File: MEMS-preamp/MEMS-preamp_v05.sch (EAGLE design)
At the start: 19 parts, among them Q1 OPA2134

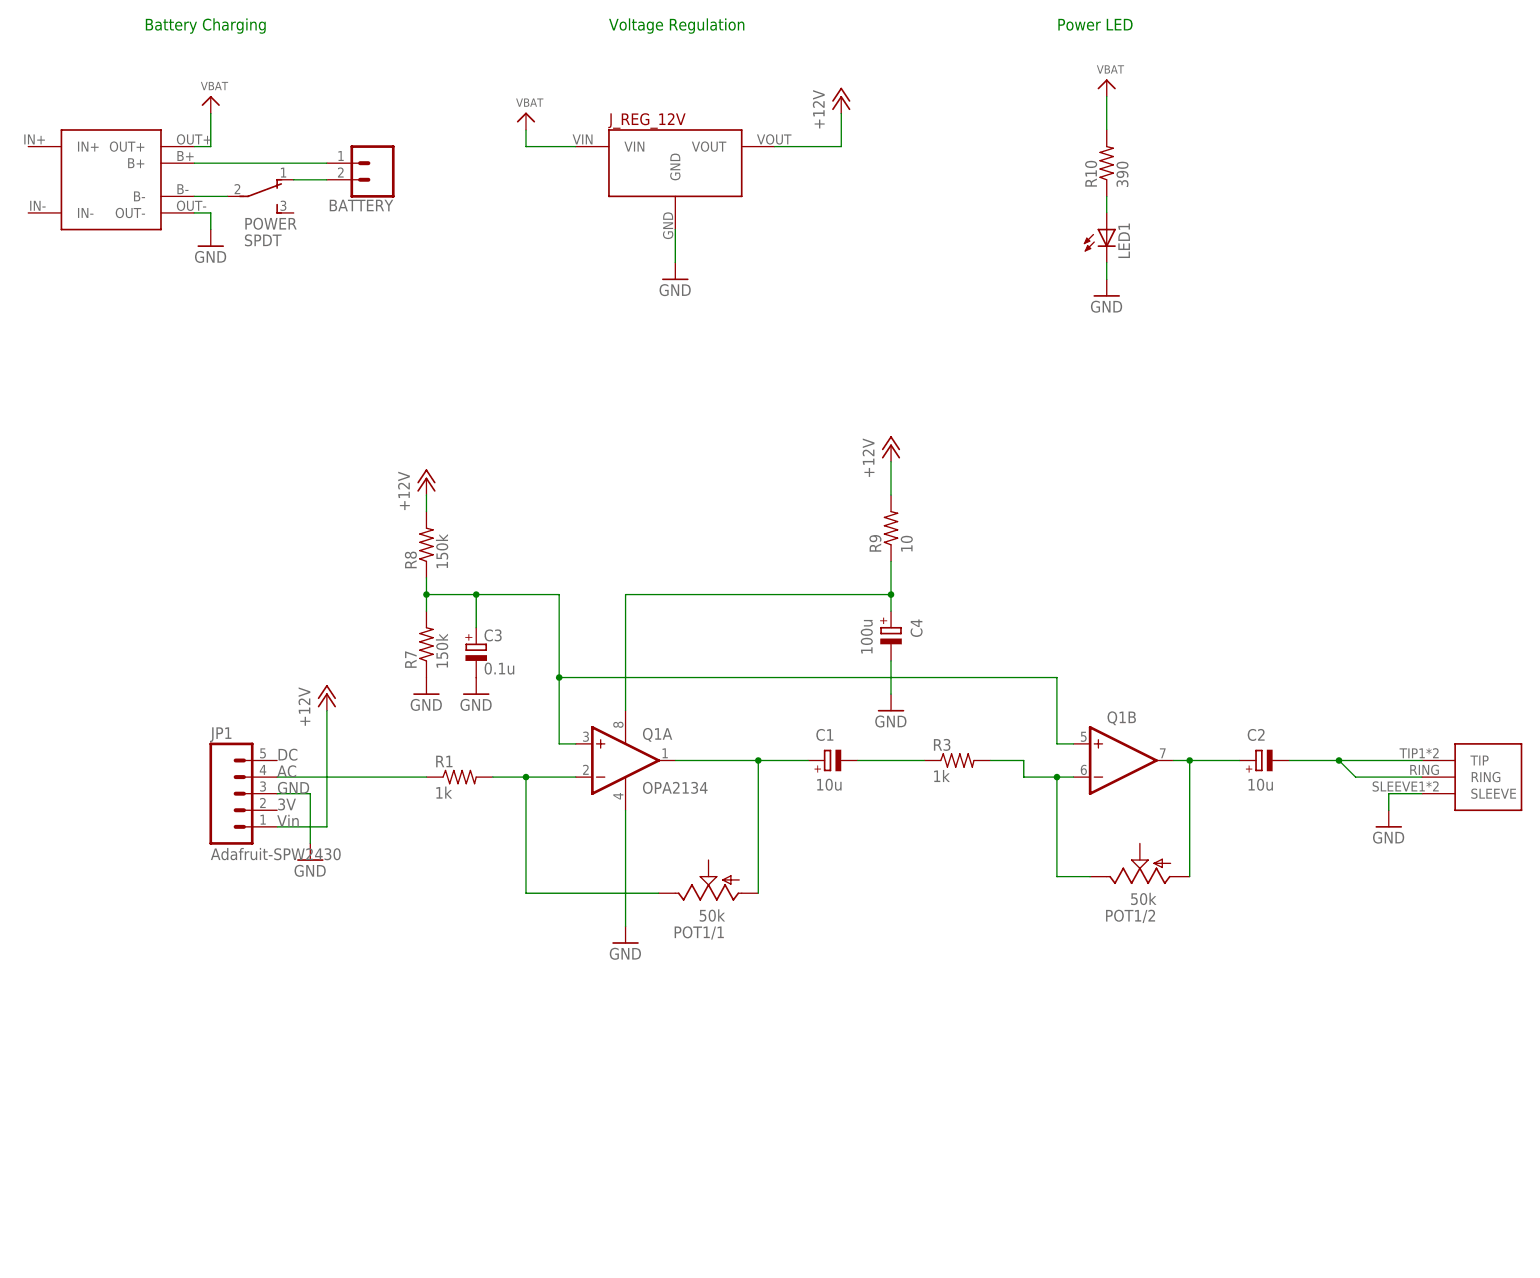
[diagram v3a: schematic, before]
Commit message: new piezo preamp designs
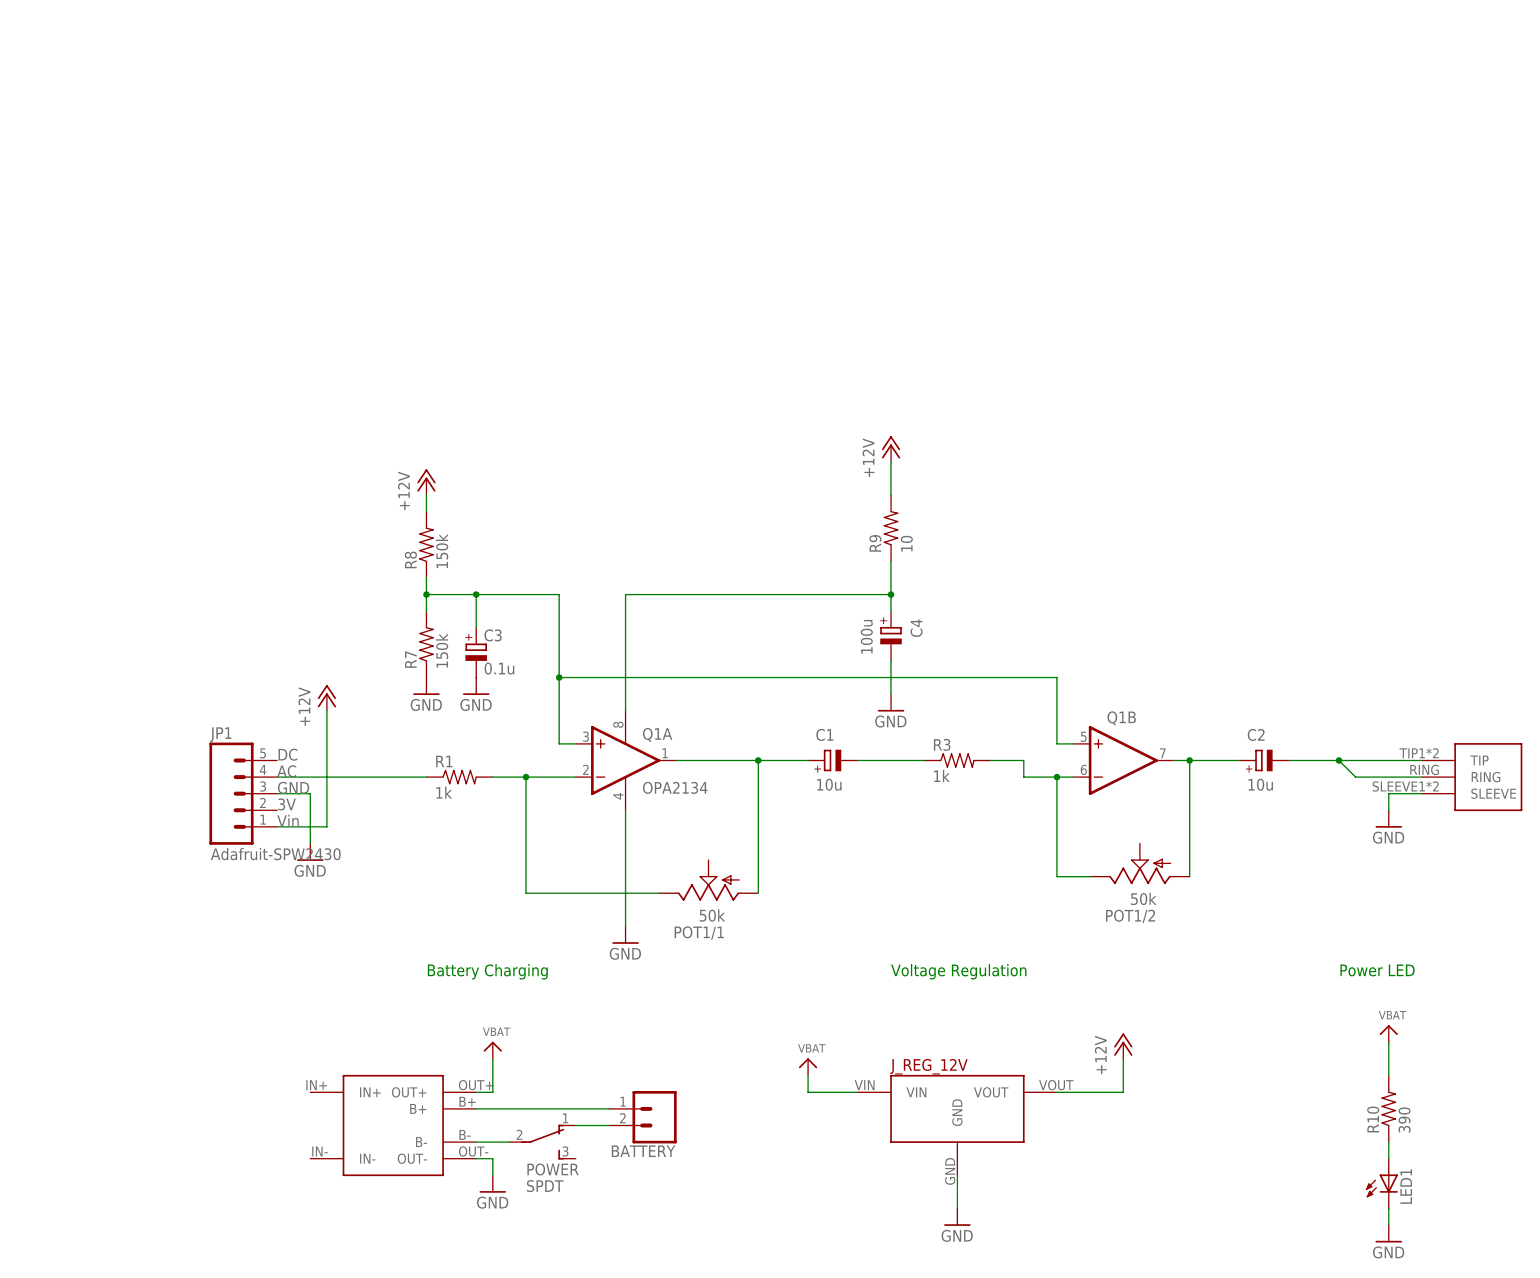
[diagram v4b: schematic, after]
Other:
- moved on the sheet: BATTERY, J_REG_12V, LED1, POWER, R10
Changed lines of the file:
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@@
 <sheet>
 <plain>
-<text x="66.04" y="182.88" size="1.778" layer="91">Voltage Regulation</text>
-<text x="-5.08" y="182.88" size="1.778" layer="91">Battery Charging</text>
-<text x="134.62" y="182.88" size="1.778" layer="91">Power LED</text>
+<text x="109.22" y="38.1" size="1.778" layer="91">Voltage Regulation</text>
+<text x="38.1" y="38.1" size="1.778" layer="91">Battery Charging</text>
+<text x="177.8" y="38.1" size="1.778" layer="91">Power LED</text>
 </plain>
 <instances>
@@
 <attribute name="VALUE" x="182.88" y="58.42" size="1.778" layer="96" ratio="12"/>
 </instance>
-<instance part="LED1" gate="G$1" x="142.24" y="152.4"/>
-<instance part="GND1" gate="1" x="142.24" y="142.24" smashed="yes">
-<attribute name="VALUE" x="139.7" y="139.7" size="1.778" layer="96" ratio="12"/>
-</instance>
-<instance part="R10" gate="G$1" x="142.24" y="162.56" rot="R90"/>
-<instance part="J_REG_12V" gate="J_REG_5V" x="76.2" y="165.1"/>
-<instance part="GND12" gate="1" x="76.2" y="144.78" smashed="yes">
-<attribute name="VALUE" x="73.66" y="142.24" size="1.778" layer="96" ratio="12"/>
-</instance>
-<instance part="U$2" gate="G$1" x="53.34" y="170.18"/>
-<instance part="P+1" gate="1" x="101.6" y="172.72"/>
-<instance part="U$3" gate="G$1" x="142.24" y="175.26"/>
+<instance part="LED1" gate="G$1" x="185.42" y="7.62"/>
+<instance part="GND1" gate="1" x="185.42" y="-2.54" smashed="yes">
+<attribute name="VALUE" x="182.88" y="-5.08" size="1.778" layer="96" ratio="12"/>
+</instance>
+<instance part="R10" gate="G$1" x="185.42" y="17.78" rot="R90"/>
+<instance part="J_REG_12V" gate="J_REG_5V" x="119.38" y="20.32"/>
+<instance part="GND12" gate="1" x="119.38" y="0" smashed="yes">
+<attribute name="VALUE" x="116.84" y="-2.54" size="1.778" layer="96" ratio="12"/>
+</instance>
+<instance part="U$2" gate="G$1" x="96.52" y="25.4"/>
+<instance part="P+1" gate="1" x="144.78" y="27.94"/>
+<instance part="U$3" gate="G$1" x="185.42" y="30.48"/>
 <instance part="P+5" gate="1" x="109.22" y="119.38"/>
-<instance part="USB-LIPO-CHARGER" gate="G$1" x="-10.16" y="160.02"/>
-<instance part="U$8" gate="G$1" x="5.08" y="172.72"/>
-<instance part="GND13" gate="1" x="5.08" y="149.86" smashed="yes">
-<attribute name="VALUE" x="2.54" y="147.32" size="1.778" layer="96" ratio="12"/>
+<instance part="USB-LIPO-CHARGER" gate="G$1" x="33.02" y="15.24"/>
+<instance part="U$8" gate="G$1" x="48.26" y="27.94"/>
+<instance part="GND13" gate="1" x="48.26" y="5.08" smashed="yes">
+<attribute name="VALUE" x="45.72" y="2.54" size="1.778" layer="96" ratio="12"/>
 </instance>
 <instance part="P+6" gate="1" x="38.1" y="114.3"/>
-<instance part="POWER" gate="G$1" x="12.7" y="157.48"/>
+<instance part="POWER" gate="G$1" x="55.88" y="12.7"/>
 <instance part="P+2" gate="1" x="22.86" y="81.28"/>
-<instance part="BATTERY" gate="G$1" x="30.48" y="162.56" rot="R180"/>
+<instance part="BATTERY" gate="G$1" x="73.66" y="17.78" rot="R180"/>
 <instance part="R3" gate="G$1" x="119.38" y="71.12"/>
 <instance part="C2" gate="G$1" x="165.1" y="71.12" smashed="yes" rot="R90">
@@
 <pinref part="LED1" gate="G$1" pin="C"/>
 <pinref part="GND1" gate="1" pin="GND"/>
-<wire x1="142.24" y1="147.32" x2="142.24" y2="144.78" width="0.1524" layer="91"/>
+<wire x1="185.42" y1="2.54" x2="185.42" y2="0" width="0.1524" layer="91"/>
 </segment>
 <segment>
 <pinref part="J_REG_12V" gate="J_REG_5V" pin="GND"/>
 <pinref part="GND12" gate="1" pin="GND"/>
-<wire x1="76.2" y1="152.4" x2="76.2" y2="147.32" width="0.1524" layer="91"/>
+<wire x1="119.38" y1="7.62" x2="119.38" y2="2.54" width="0.1524" layer="91"/>
 </segment>
 <segment>
 <pinref part="USB-LIPO-CHARGER" gate="G$1" pin="OUT-"/>
 <pinref part="GND13" gate="1" pin="GND"/>
-<wire x1="2.54" y1="154.94" x2="5.08" y2="154.94" width="0.1524" layer="91"/>
-<wire x1="5.08" y1="154.94" x2="5.08" y2="152.4" width="0.1524" layer="91"/>
+<wire x1="45.72" y1="10.16" x2="48.26" y2="10.16" width="0.1524" layer="91"/>
+<wire x1="48.26" y1="10.16" x2="48.26" y2="7.62" width="0.1524" layer="91"/>
 </segment>
 </net>
@@
 <pinref part="U$2" gate="G$1" pin="VBAT"/>
 <pinref part="J_REG_12V" gate="J_REG_5V" pin="VIN"/>
-<wire x1="53.34" y1="167.64" x2="53.34" y2="165.1" width="0.1524" layer="91"/>
-<wire x1="53.34" y1="165.1" x2="60.96" y2="165.1" width="0.1524" layer="91"/>
+<wire x1="96.52" y1="22.86" x2="96.52" y2="20.32" width="0.1524" layer="91"/>
+<wire x1="96.52" y1="20.32" x2="104.14" y2="20.32" width="0.1524" layer="91"/>
 </segment>
 <segment>
 <pinref part="R10" gate="G$1" pin="2"/>
 <pinref part="U$3" gate="G$1" pin="VBAT"/>
-<wire x1="142.24" y1="167.64" x2="142.24" y2="172.72" width="0.1524" layer="91"/>
+<wire x1="185.42" y1="22.86" x2="185.42" y2="27.94" width="0.1524" layer="91"/>
 </segment>
 <segment>
 <pinref part="USB-LIPO-CHARGER" gate="G$1" pin="OUT+"/>
 <pinref part="U$8" gate="G$1" pin="VBAT"/>
-<wire x1="2.54" y1="165.1" x2="5.08" y2="165.1" width="0.1524" layer="91"/>
-<wire x1="5.08" y1="165.1" x2="5.08" y2="170.18" width="0.1524" layer="91"/>
+<wire x1="45.72" y1="20.32" x2="48.26" y2="20.32" width="0.1524" layer="91"/>
+<wire x1="48.26" y1="20.32" x2="48.26" y2="25.4" width="0.1524" layer="91"/>
 </segment>
 </net>
@@
 <pinref part="R10" gate="G$1" pin="1"/>
 <pinref part="LED1" gate="G$1" pin="A"/>
-<wire x1="142.24" y1="157.48" x2="142.24" y2="154.94" width="0.1524" layer="91"/>
+<wire x1="185.42" y1="12.7" x2="185.42" y2="10.16" width="0.1524" layer="91"/>
 </segment>
 </net>
@@
 <segment>
 <pinref part="J_REG_12V" gate="J_REG_5V" pin="VOUT"/>
-<wire x1="91.44" y1="165.1" x2="101.6" y2="165.1" width="0.1524" layer="91"/>
-<wire x1="101.6" y1="165.1" x2="101.6" y2="170.18" width="0.1524" layer="91"/>
+<wire x1="134.62" y1="20.32" x2="144.78" y2="20.32" width="0.1524" layer="91"/>
+<wire x1="144.78" y1="20.32" x2="144.78" y2="25.4" width="0.1524" layer="91"/>
 <pinref part="P+1" gate="1" pin="+12V"/>
 </segment>
@@
 <segment>
 <pinref part="USB-LIPO-CHARGER" gate="G$1" pin="B+"/>
-<wire x1="2.54" y1="162.56" x2="22.86" y2="162.56" width="0.1524" layer="91"/>
+<wire x1="45.72" y1="17.78" x2="66.04" y2="17.78" width="0.1524" layer="91"/>
 <pinref part="BATTERY" gate="G$1" pin="1"/>
 </segment>
@@
 <segment>
 <pinref part="USB-LIPO-CHARGER" gate="G$1" pin="B-"/>
-<wire x1="7.62" y1="157.48" x2="2.54" y2="157.48" width="0.1524" layer="91"/>
+<wire x1="50.8" y1="12.7" x2="45.72" y2="12.7" width="0.1524" layer="91"/>
 <pinref part="POWER" gate="G$1" pin="2"/>
 </segment>
@@
 <segment>
 <pinref part="POWER" gate="G$1" pin="1"/>
-<wire x1="17.78" y1="160.02" x2="22.86" y2="160.02" width="0.1524" layer="91"/>
+<wire x1="60.96" y1="15.24" x2="66.04" y2="15.24" width="0.1524" layer="91"/>
 <pinref part="BATTERY" gate="G$1" pin="2"/>
 </segment>
